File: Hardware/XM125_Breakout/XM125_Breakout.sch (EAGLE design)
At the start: 2 parts

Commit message: Removed uneeded board files; updates to breakout board
Removed the 1x1 and Thing+ board options; updated the schematic and layout - grouped together the needed sections in the layout
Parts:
- removed FRAME1: FRAME-LEDGER, SparkFun-Aesthetics:FRAME-LEDGER
- added 3V3, JP2, SHLD: JUMPER-SMT_2_NC_TRACE_SILK, SparkFun-Jumpers:JUMPER-SMT_2_NC_TRACE_SILK
- added C1, C11, C2, C3, C6, C8: 22uF, SparkFun-Capacitors:22UF-0603-6.3V-20%
- added C10, C5: 1.0uF, SparkFun-Capacitors:1.0UF-0603-16V-10%-X7R
- added C12: 10nF, SparkFun-Capacitors:10NF-0603-50V-10%
- added C13: 10uF, SparkFun-Capacitors:10UF-POLAR-0603-6.3V-20%(TANT)
- added C14, C15: 0.1uF, SparkFun-Capacitors:0.1UF-0603-25V-(+80/-20%)
- added C4, C9: 0.1uF, SparkFun-Capacitors:0.1UF-0603-25V-5%
- added C7: 22pF, SparkFun-Capacitors:22PF-0603-50V-5%
- added D1: Red, SparkFun-LED:LED-RED_0603-KB
- added FRAME2: FRAME-LETTER, SparkFun-Aesthetics:FRAME-LETTER
- added I2C: JUMPER-SMT_3_2-NC_TRACE_SILK, SparkFun-Jumpers:JUMPER-SMT_3_2-NC_TRACE_SILK
- added J1: (no value), SparkFun-Connectors:USB_C_2-LAYER_PADS
- added J2, J3: QWIIC_RIGHT_ANGLE, SparkFun-Connectors:QWIIC_CONNECTORJS-1MM
- added J4: (no value), SparkFun-Connectors:CONN_031X03_NO_SILK
- added J5, J6: (no value), SparkFun-Connectors:CONN_021X02_NO_SILK
- added J7, J8: (no value), SparkFun-Connectors:CONN_041X04_NO_SILK
- added J9: (no value), SparkFun-Connectors:CONN_01PTH_NO_SILK_STAND
- added L1, L2: 2.2μH, SparkFun-Coils:2.2μH-4X4-2.2μH-3A-45MOHM
- added LOGO2: QWIIC_LOGO_3MM, SparkFun-Aesthetics:QWIIC_LOGO_3MM
- added LOGO3: SFE_LOGO_NAME_FLAME.1_INCH, SparkFun-Aesthetics:SFE_LOGO_NAME_FLAME.1_INCH
- added LOGO4: OSHW-LOGOS, SparkFun-Aesthetics:OSHW-LOGOS
- added LOGO5: SFE_LOGO_FLAME.1_INCH, SparkFun-Aesthetics:SFE_LOGO_FLAME.1_INCH
- added LOGO6: SFE_LOGO_NAME.1_INCH, SparkFun-Aesthetics:SFE_LOGO_NAME.1_INCH
- added R1, R4, R6: 100k, SparkFun-Resistors:100KOHM-0603-1/10W-1%
- added R10: 1k, SparkFun-Resistors:1KOHM-0603-1/10W-1%
- added R11, R12: 2.2k, SparkFun-Resistors:2.2KOHM-0603-1/10W-1%
- added R13: 10k, SparkFun-Resistors:10KOHM-0603-1/10W-1%
- added R2: 300k, SparkFun-Resistors:300KOHM-0603-1/10W-1%
- added R3: 150k, SparkFun-Resistors:150KOHM-0603-1/10W-1%
- added R5: 453k, SparkFun-Resistors:453KOHM-0603-1/10W-1%
- added R7, R8: 5.1k, SparkFun-Resistors:5.1KOHM5.1KOHM-0603-1/10W-1%
- added S1, S2: (no value), SparkFun-Switches:MOMENTARY-SWITCH-SPST-2-SMD-5.2MM-TALL
- added U1: XM125, XM125:XM125
- added U2, U3: (no value), SparkFun-IC-Power:AP3429/A
- added U4: CH340C, SparkFun-IC-Comms:CH340C
- added U5: ESD Diode, SparkFun-DiscreteSemi:TVS_DIODE_ARRAY_DT1042-04SO-7
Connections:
- new net 1.8V: C11.1, C2.1, C3.1, C4.1, C5.1, J7.4, L1.2, R2.2, U1.1V8
- new net 3.3V: 3V3.2, C10.1, C15.1, C7.1, C8.1, C9.1, I2C.2, J2.2, J3.2, J7.3, JP2.2, L2.2, R5.2, S2.3, S2.4, U1.VIN, U4.VCC
- new net CH340-CTS: U1.UART_CTS, U4.!CTS
- new net CH340-RTS: U1.UART_RTS, U4.!RTS
- new net CH340-RX: U1.UART_TX, U4.RXI
- new net CH340-TX: U1.UART_RX, U4.TXO
- new net DEBUG_UART-RX: J5.1, U1.DEBUG_UART_RX
- new net DEBUG_UART-TX: J5.2, U1.DEBUG_UART_TX
- new net GND: C1.2, C10.2, C11.2, C12.2, C13.-, C14.2, C15.2, C3.2, C4.2, C5.2, C6.2, C8.2, C9.2, D1.C, J1.GND, J2.1, J3.1, J7.1, J7.2, R11.1, R12.1, R3.2, R6.1, R7.1, R8.1, SHLD.1, U1.GND, U2.GND, U3.GND, U4.GND, U5.VSS
- new net INT: J4.1
- new net N$1: J1.D+, U4.UD+, U5.IO3
- new net N$10: J1.CC2, R8.2
- new net N$11: J1.CC1, R7.2
- new net N$12: C12.1, U4.V3
- new net N$14: 3V3.1, R10.2
- new net N$15: D1.A, R10.1
- new net N$16: I2C.3, R11.2
- new net N$17: I2C.1, R12.2
- new net N$18: JP2.1, R13.2
- new net N$19: S1.3, S1.4
- new net N$2: J1.D-, U4.UD-, U5.IO4
- new net N$3: L1.1, U2.LX
- new net N$4: R1.2, U2.EN
- new net N$5: R4.2, U3.EN
- new net N$6: C2.2, R2.1, R3.1, U2.FB
- new net N$7: L2.1, U3.LX
- new net N$8: C7.2, R5.1, R6.2, U3.FB
- new net N$9: J1.SHLD, SHLD.2
- new net SCL: J2.4, J3.4, J4.3, U1.SCL
- new net SDA: J2.3, J3.3, J4.2, U1.SDA
- new net SWD_CLK: J6.2, U1.SWD_CLK
- new net SWD_IO: J6.1, U1.SWD_IO
- new net V_USB: C1.1, C13.+, C14.1, C6.1, J1.VBUS, R1.1, R4.1, U2.VIN, U3.VIN, U5.VCC
- new net WAKE_UP: U1.WAKE_UP
- new net XM125_GPIO0: J8.1, U1.MISC_GPIO0
- new net XM125_GPIO1: J8.2, U1.MISC_GPIO1
- new net XM125_GPIO2/BOOT0: J8.3, S2.1, S2.2, U1.MISC_GPIO2_BOOT0
- new net XM125_INT: J8.4, R13.1, U1.MCU_INT
- new net XM125_RESET: J9.1, S1.1, S1.2, U1.RESET
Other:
- note added: "1.8V Buck Regulator - AP3429A"
- note added: "3.3V Buck Regulator - AP3429A"
- note added: "Boot and Reset Buttons"
- note added: "Breakout Headers"
- note added: "Cut trace to remove pullup"
- note added: "INT"
- note added: "INT Pullup"
- note added: "I²C Pullup"
- note added: "Power LED"
- note added: "Qwiic Connector"
- note added: "USB-to-Serial Converter"
- note added: "XM125 - A121 Breakout"

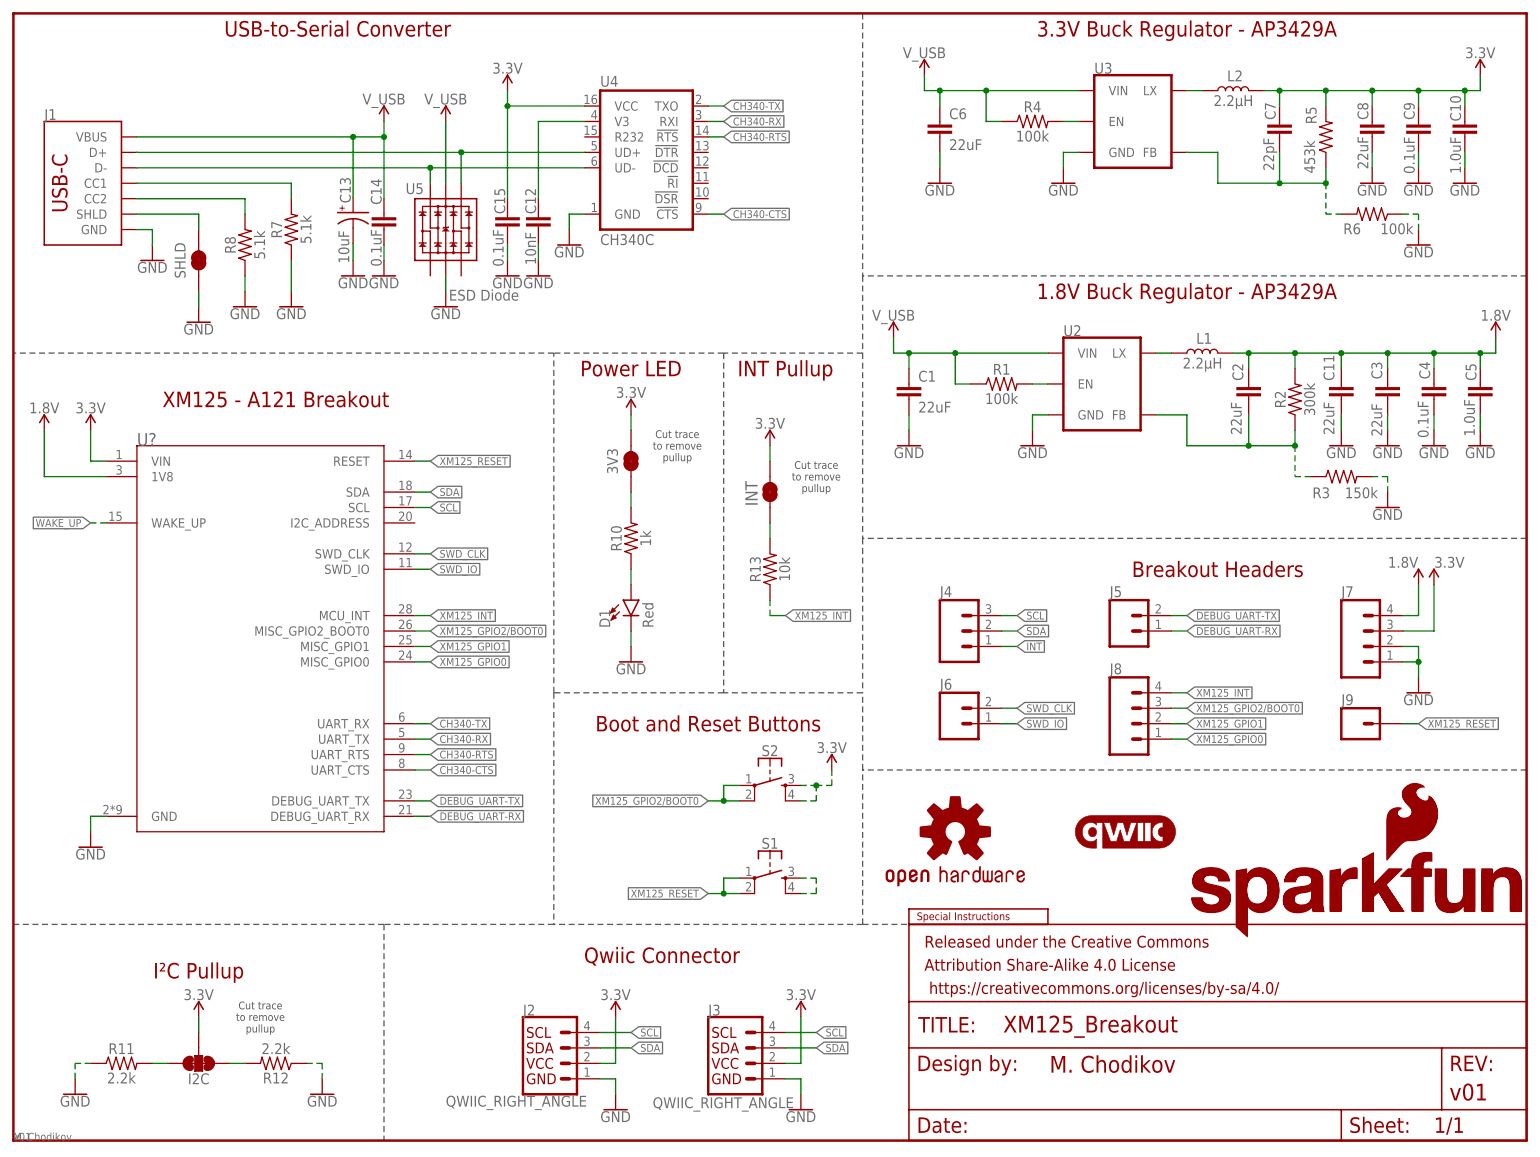
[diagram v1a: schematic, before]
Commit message: Addition of further documentation; initial schematic ready for review
Fixed small issues on schematic; added I2C documentation to the repo
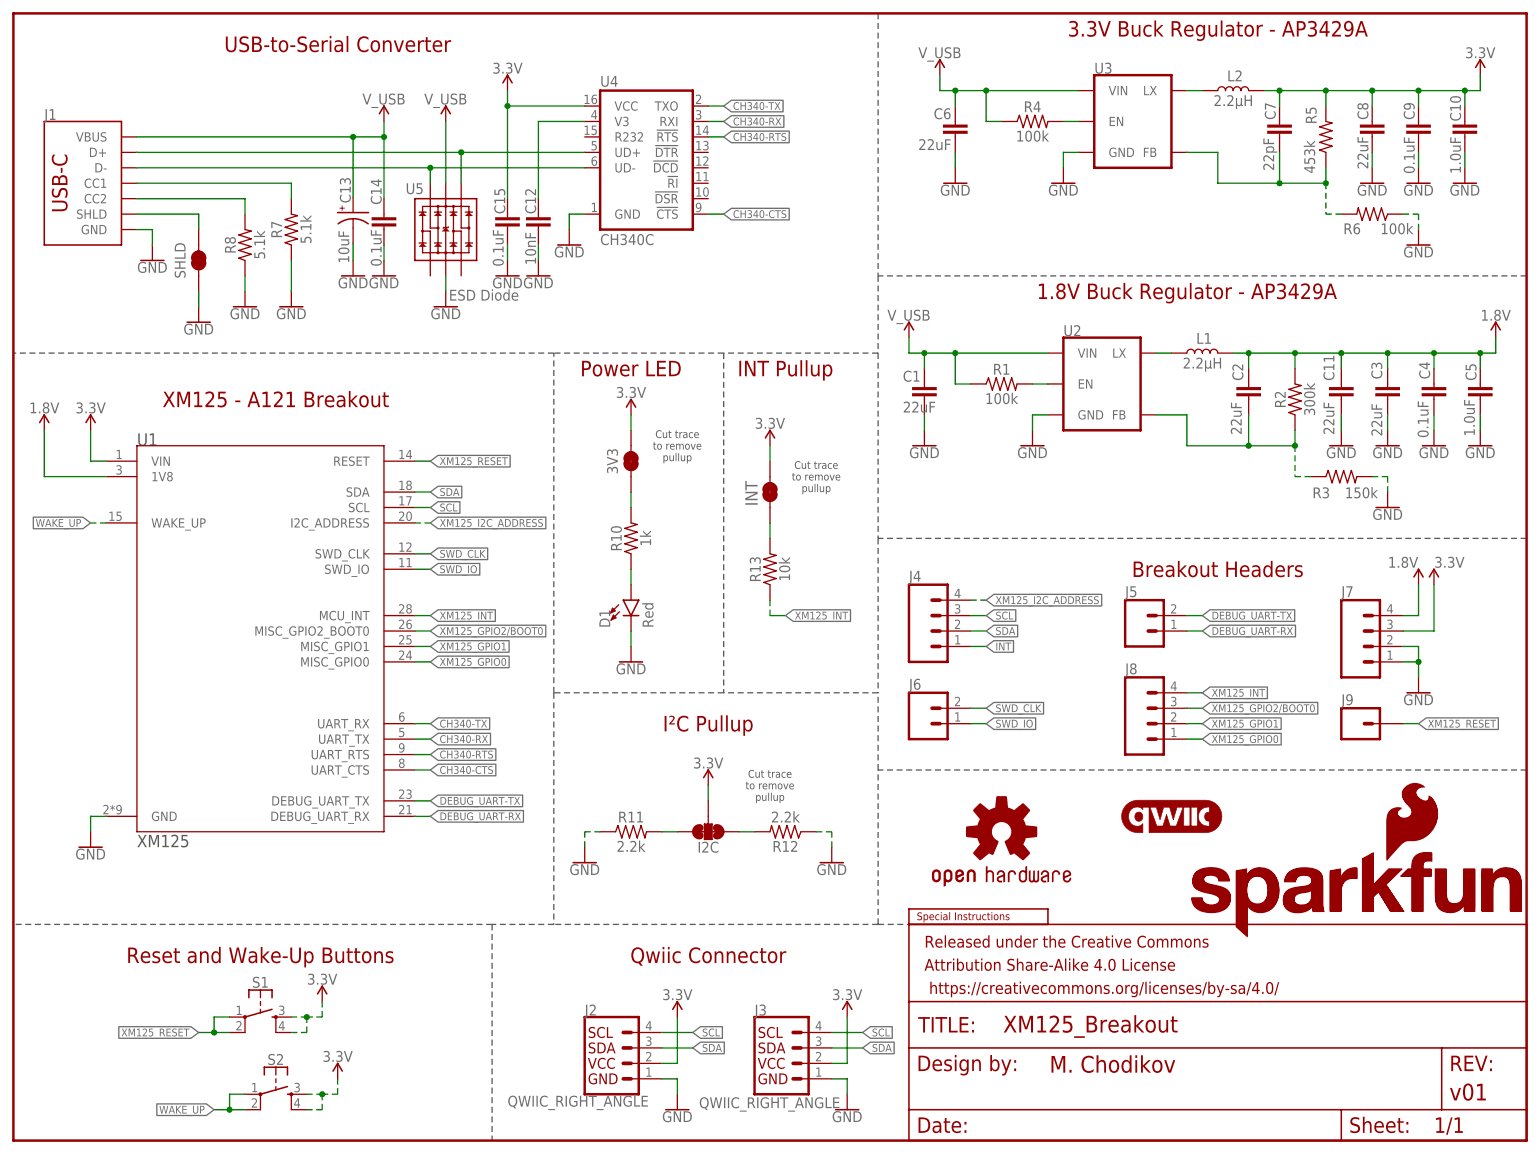
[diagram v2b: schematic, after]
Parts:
- J4: device SparkFun-Connectors:CONN_031X03_NO_SILK -> SparkFun-Connectors:CONN_041X04_NO_SILK
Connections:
- removed net N$19: S1.3, S1.4
- new net XM125_I2C_ADDRESS: J4.4, U1.I2C_ADDRESS
- net 3.3V: now also S1.3, S1.4
- net WAKE_UP: now also S2.1, S2.2
- net XM125_GPIO2/BOOT0: no longer S2.1, S2.2
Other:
- note added: "Reset and Wake-Up Buttons"
- note added: "U1"
- note added: "XM125"
- note removed: "Boot and Reset Buttons"
- moved on the sheet: C1, C6, I2C, J2, J3, J5, J6, J8, R11, R12, S1, S2

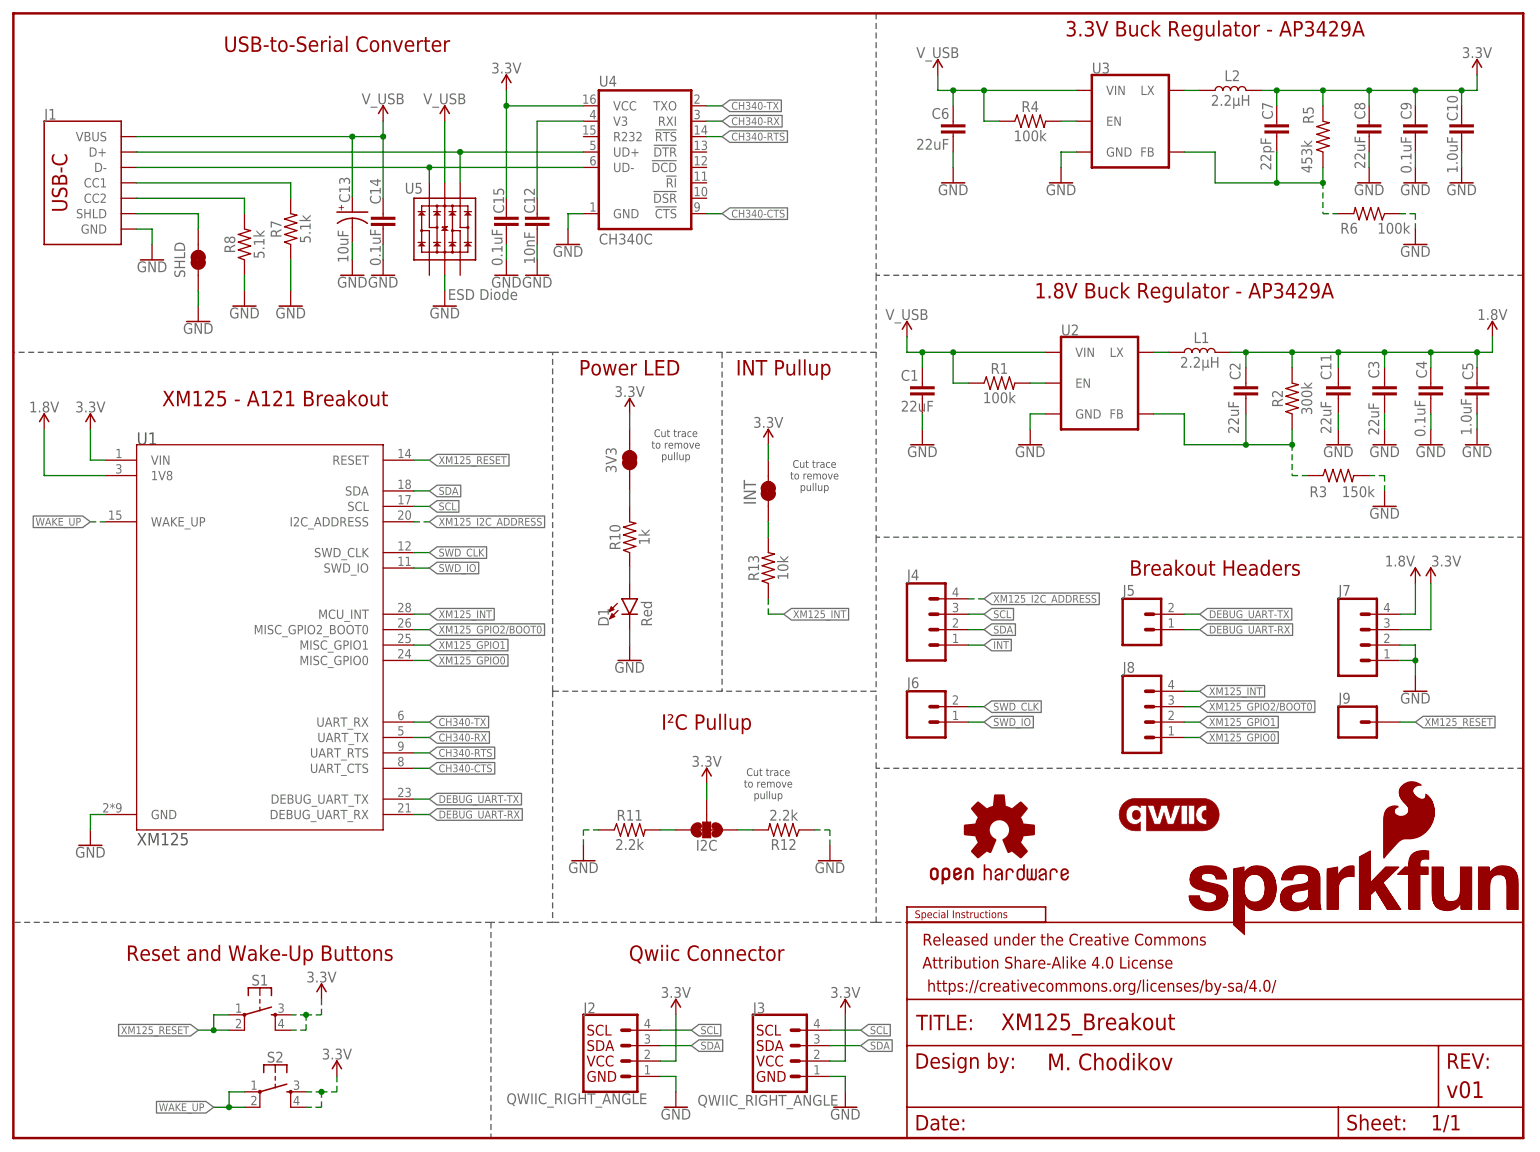
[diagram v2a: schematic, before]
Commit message: Updates as per schematic review
For full detailed list of changes, see XM125 Schematic review document
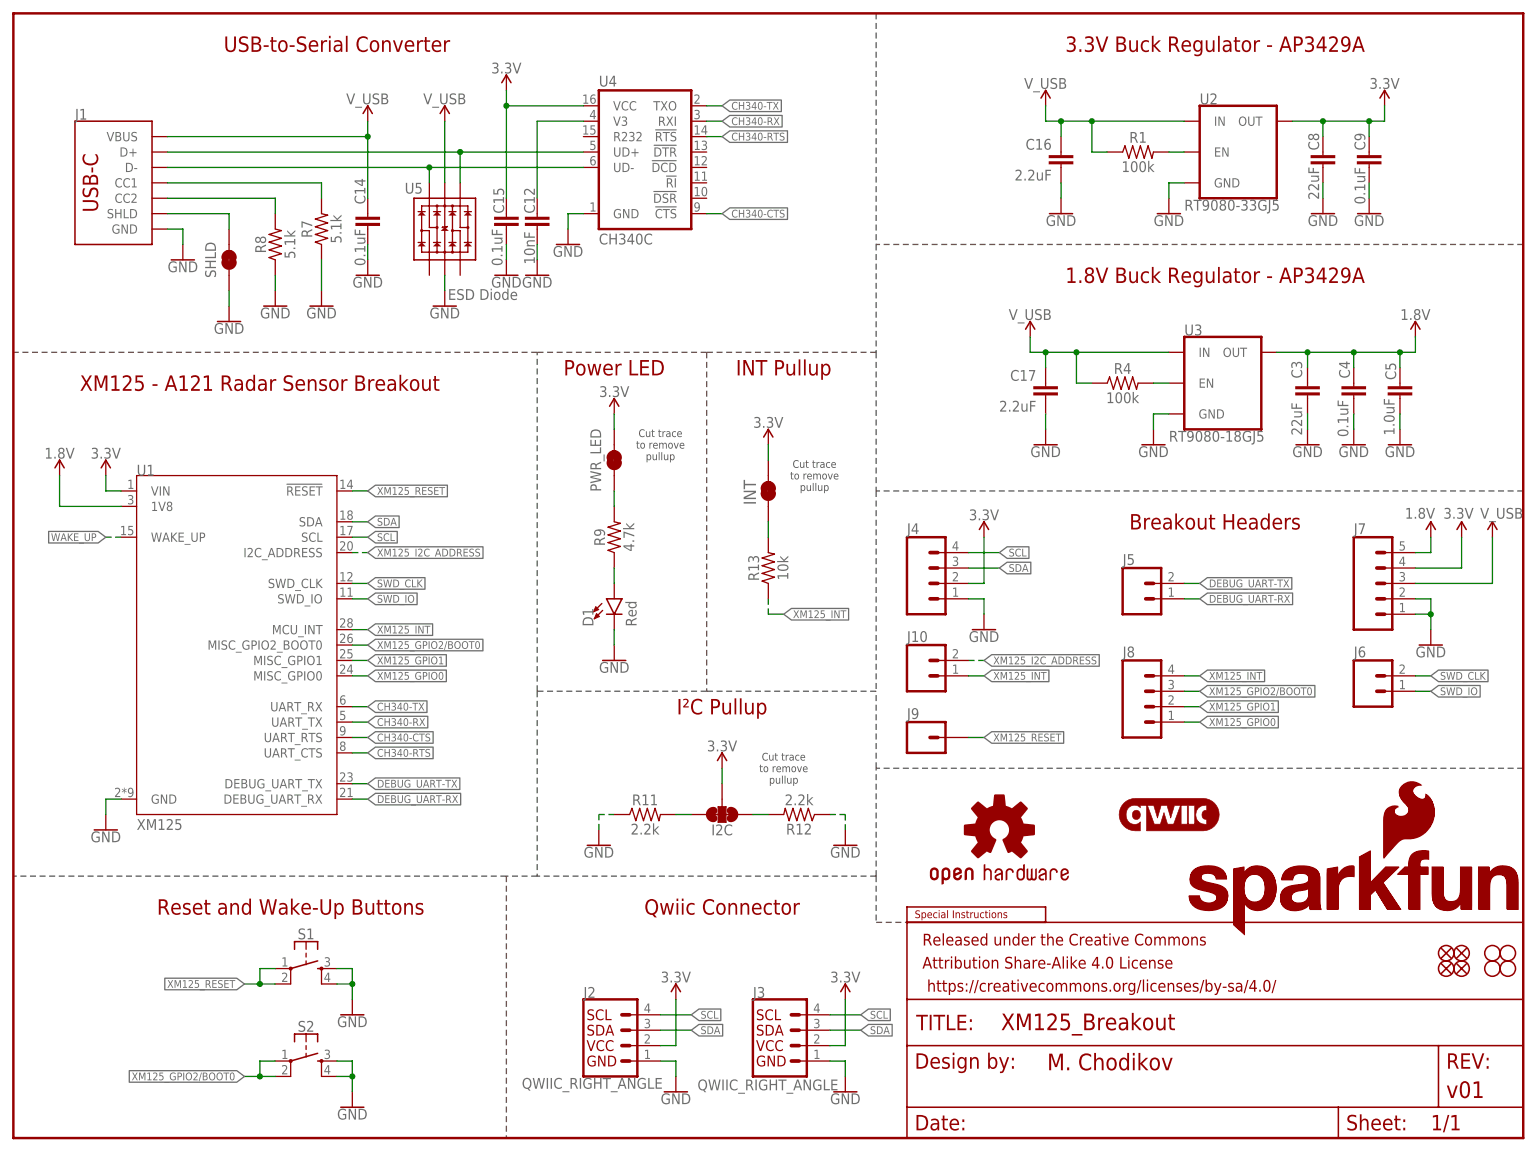
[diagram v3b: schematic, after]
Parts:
- removed 3V3: JUMPER-SMT_2_NC_TRACE_SILK, SparkFun-Jumpers:JUMPER-SMT_2_NC_TRACE_SILK
- removed C1, C11, C2, C6: 22uF, SparkFun-Capacitors:22UF-0603-6.3V-20%
- removed C10: 1.0uF, SparkFun-Capacitors:1.0UF-0603-16V-10%-X7R
- removed C13: 10uF, SparkFun-Capacitors:10UF-POLAR-0603-6.3V-20%(TANT)
- removed C7: 22pF, SparkFun-Capacitors:22PF-0603-50V-5%
- removed L1, L2: 2.2μH, SparkFun-Coils:2.2μH-4X4-2.2μH-3A-45MOHM
- removed R10: 1k, SparkFun-Resistors:1KOHM-0603-1/10W-1%
- removed R2: 300k, SparkFun-Resistors:300KOHM-0603-1/10W-1%
- removed R3: 150k, SparkFun-Resistors:150KOHM-0603-1/10W-1%
- removed R5: 453k, SparkFun-Resistors:453KOHM-0603-1/10W-1%
- removed R6: 100k, SparkFun-Resistors:100KOHM-0603-1/10W-1%
- added C16, C17: 2.2uF, SparkFun-Capacitors:2.2UF-0603-10V-20%
- added FD1, FD2, FD3, FD4: FIDUCIAL1X2, SparkFun-Aesthetics:FIDUCIAL1X2
- added H1, H2, H3, H4: STAND-OFF, SparkFun-Hardware:STAND-OFF
- added J10: (no value), SparkFun-Connectors:CONN_021X02_NO_SILK
- added PWR_LED: JUMPER-SMT_2_NC_TRACE_SILK, SparkFun-Jumpers:JUMPER-SMT_2_NC_TRACE_SILK
- added R9: 4.7k, SparkFun-Resistors:4.7KOHM-0603-1/10W-1%
- J7: device SparkFun-Connectors:CONN_041X04_NO_SILK -> SparkFun-Connectors:CONN_05NO_SILK
- U2: value (none) -> RT9080-33GJ5; device SparkFun-IC-Power:AP3429/A -> SparkFun-IC-Power:V_REG_RT9080
- U3: value (none) -> RT9080-18GJ5; device SparkFun-IC-Power:AP3429/A -> XM125:RT9080-18GJ5
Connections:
- removed net INT: J4.1
- removed net N$3: L1.1, U2.LX
- removed net N$6: C2.2, R2.1, R3.1, U2.FB
- removed net N$7: L2.1, U3.LX
- removed net N$8: C7.2, R5.1, R6.2, U3.FB
- net 1.8V: now also J7.5, U3.OUT; no longer C11.1, C2.1, J7.4, L1.2, R2.2
- net 3.3V: now also J4.2, J7.4, PWR_LED.2, U2.OUT; no longer 3V3.2, C10.1, C7.1, J7.3, L2.2, R5.2, S1.3, S1.4, S2.3, S2.4
- net CH340-CTS: now also U1.UART_RTS; no longer U1.UART_CTS
- net CH340-RTS: now also U1.UART_CTS; no longer U1.UART_RTS
- net GND: now also C16.2, C17.2, J4.1, S1.3, S1.4, S2.3, S2.4; no longer C1.2, C10.2, C11.2, C13.-, C6.2, R3.2, R6.1
- net N$14: now also PWR_LED.1, R9.2; no longer 3V3.1, R10.2
- net N$15: now also R9.1; no longer R10.1
- net SCL: now also J4.4; no longer J4.3
- net SDA: now also J4.3; no longer J4.2
- net V_USB: now also C16.1, C17.1, J7.3, U2.IN, U3.IN; no longer C1.1, C13.+, C6.1, U2.VIN, U3.VIN
- net WAKE_UP: no longer S2.1, S2.2
- net XM125_GPIO2/BOOT0: now also S2.1, S2.2
- net XM125_I2C_ADDRESS: now also J10.2; no longer J4.4
- net XM125_INT: now also J10.1
- net XM125_RESET: now also U1.!RESET; no longer U1.RESET
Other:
- note added: "XM125 - A121 Radar Sensor Breakout"
- note removed: "U1"
- note removed: "XM125"
- note removed: "XM125 - A121 Breakout"
- moved on the sheet: C14, C3, C4, C5, C8, C9, D1, I2C, J1, J2, J3, J4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
